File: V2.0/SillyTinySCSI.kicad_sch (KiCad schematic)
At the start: 26 parts, among them J1 DB25_Plug, U1 74LVT125, U2 74LVT245, U3 74LVT125, U4 74LVT245

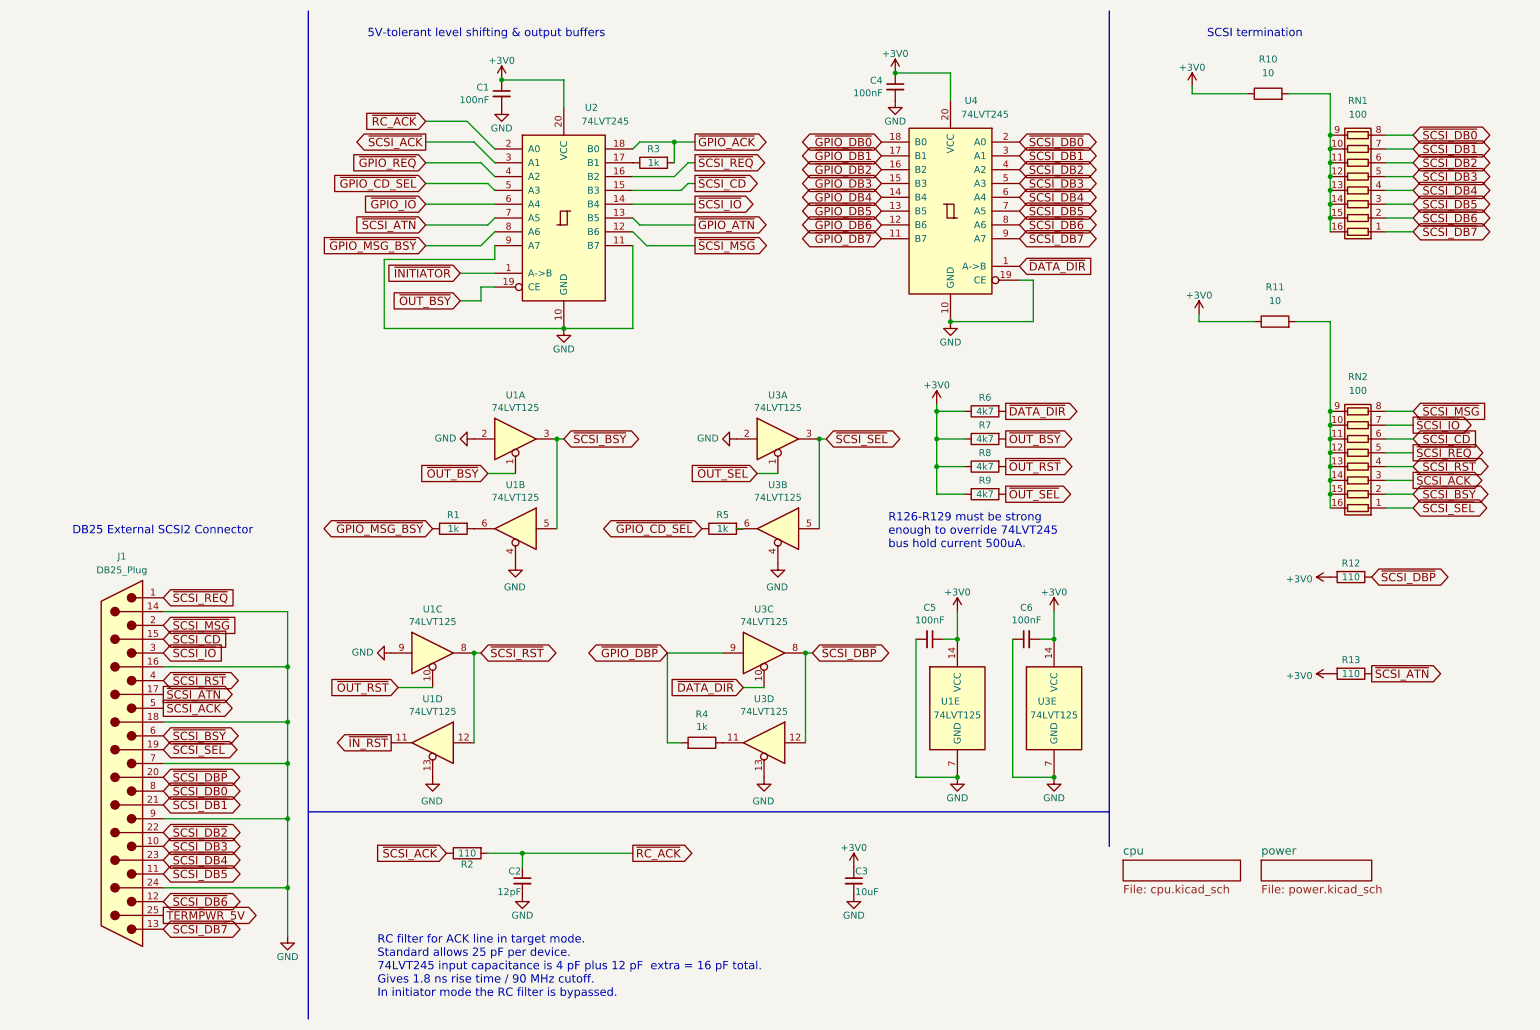
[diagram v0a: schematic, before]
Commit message: optimizations to buffers
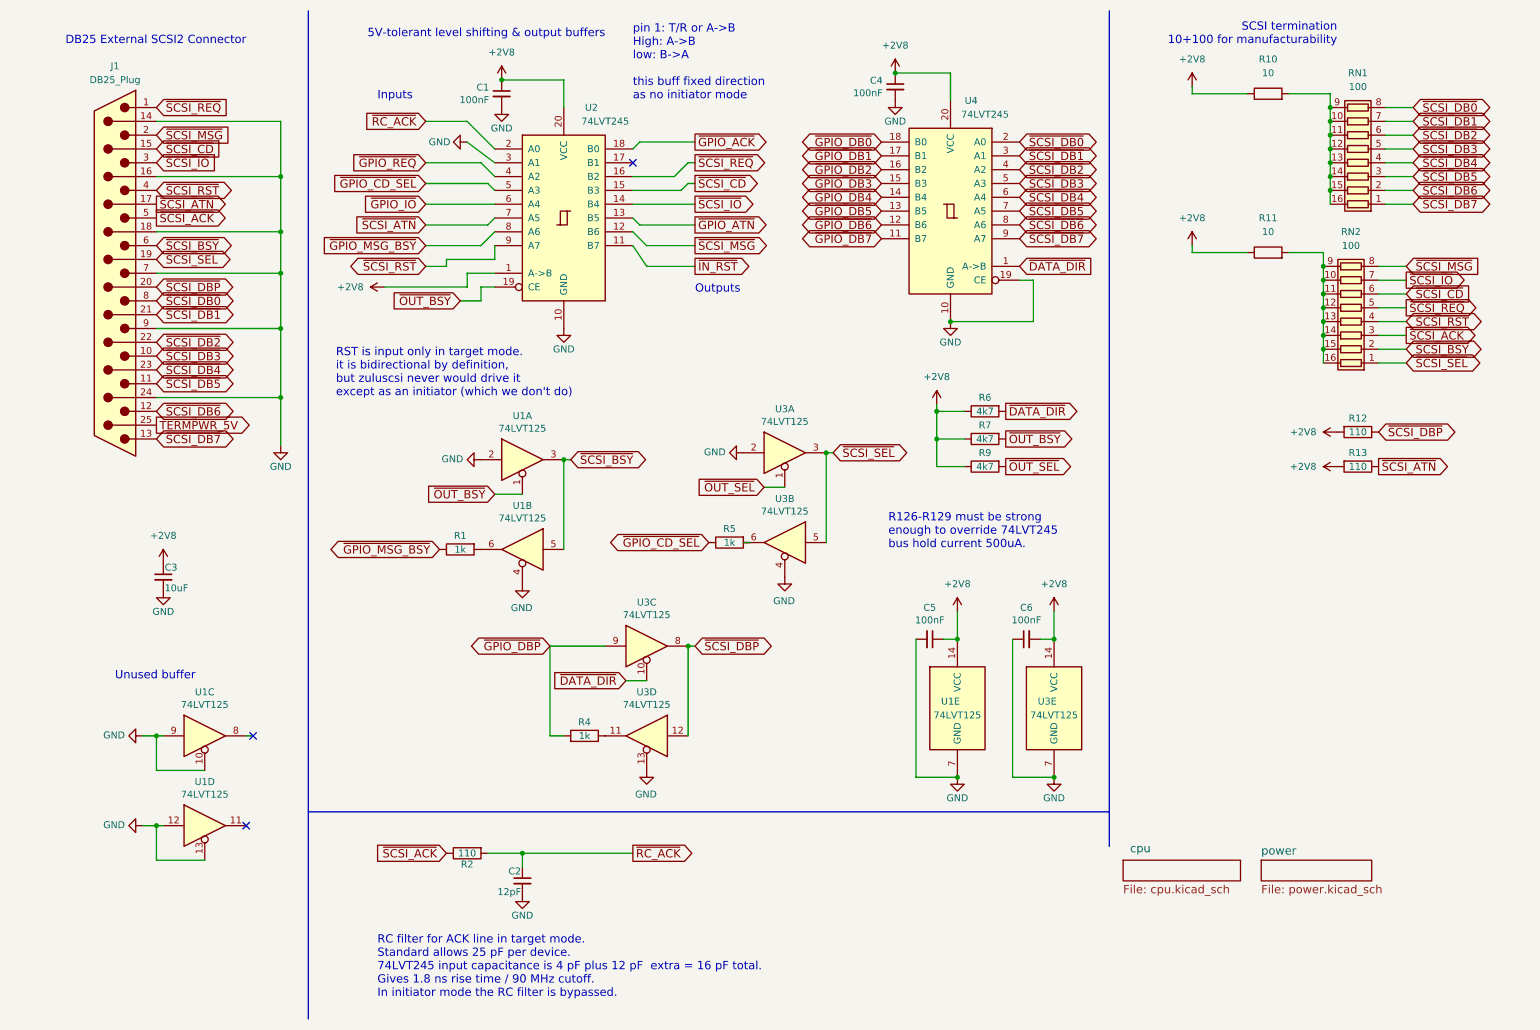
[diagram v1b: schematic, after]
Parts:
- removed R3: 1k, Resistor_SMD:R_0603_1608Metric, symbol zuluscsi-rescue:R
- removed R8: 4k7, Resistor_SMD:R_0603_1608Metric, symbol zuluscsi-rescue:R
- R10, R11: footprint Resistor_SMD:R_0603_1608Metric -> Resistor_SMD:R_1206_3216Metric; LCSC C22859 -> C727983; PartNumber 0603WAF100JT5E -> AC0805FR-7W10RL; digikey (none) -> 13-AC0805FR-7W10RLCT-ND
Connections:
- net ~{INITIATOR} is gone; now on net +2V8: U2.1 (A->B)
- net ~{OUT_RST} is gone; now on net GND: U1.10
- net GND: now also U1.12, U2.3 (A1); no longer U2.11 (B7), U2.9 (A7)
- net ~{IN_RST}: now also U2.11 (B7); no longer U1.11
- net ~{SCSI_ACK}: no longer U2.3 (A1)
- net ~{SCSI_RST}: now also U2.9 (A7); no longer U1.12, U1.8
- net +3V0 renamed +2V8
- no-connect marks 0 -> 3
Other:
- note added: "Inputs"
- note added: "Outputs"
- note added: "RST is input only in target mode. it is bidirectional by definition, but zuluscsi never would drive it except as an initiator (which we don't do)"
- note added: "SCSI termination 10+100 for manufacturability"
- note added: "Unused buffer"
- note added: "pin 1: T/R or A->B High: A->B low: B->A this buff fixed direction as no initiator mode"
- note removed: "SCSI termination"
- company: (C) Rabbit Hole Computing  -> ZZJ / M.D.
- title: ZuluSCSI (TM) Pico OSHW -> SillyTinySCSI
- moved on the sheet: C3, J1, R1, R11, R12, R13, R4, R5, R9, RN1, RN2, U1A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

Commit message: reverted some nuffer changes
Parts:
- R10, R11: LCSC C727983 -> C17903; PartNumber AC0805FR-7W10RL -> 1206W4F100JT5E; digikey 13-AC0805FR-7W10RLCT-ND -> RMCF1206JG10R0CT-ND
- RN1, RN2: digikey 13-YC248-JR-07100RLCT-ND -> RMCF0603FT51R0CT-ND - Cut Tape (CT)
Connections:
- net GND: now also U2.9 (A7); no longer U1.12
- net ~{IN_RST}: now also U1.11; no longer U2.11 (B7)
- net ~{SCSI_RST}: now also U1.12; no longer U2.9 (A7)
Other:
- note added: "Input"
- note added: "pin 1: T/R or A->B High: A->B low: B->A fixed direction as no initiator mode"
- note removed: "Inputs"
- note removed: "pin 1: T/R or A->B High: A->B low: B->A this buff fixed direction as no initiator mode"
- moved on the sheet: C3, R1, R4, R5, U1A, U1B, U1C, U3A, U3B, U3C, U3D

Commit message: last resistor pack
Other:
- moved on the sheet: C4

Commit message: before ar
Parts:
- removed R10, R11: 10, Resistor_SMD:R_1206_3216Metric, symbol Device:R
- removed RN1, RN2: 100, Resistor_SMD:R_Array_Convex_8x0602, symbol Device:R_Pack08
- added C14, C15: 10uF, Capacitor_SMD:C_0805_2012Metric, symbol zuluscsi-rescue:C_Small
- added R10, R11, R14, R21, R22, R23, R24, R25, R26, R27, R28, R29, R3, R30, R31, R8: 110, Resistor_SMD:R_0603_1608Metric, symbol zuluscsi-rescue:R
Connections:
- net +2V8: now also C14.1, C15.1, R10.2, R11.2, R14.2, R21.2, R22.2, R23.2, R24.2, R25.2, R26.2, R27.2, R28.2, R29.2, R3.2, R30.2, R31.2, R8.2
- net GND: now also C14.2, C15.2
- net ~{SCSI_ACK}: now also R21.1
- net ~{SCSI_BSY}: now also R22.1
- net ~{SCSI_CD}: now also R10.1
- net ~{SCSI_DB0}: now also R24.1
- net ~{SCSI_DB1}: now also R25.1
- net ~{SCSI_DB2}: now also R26.1
- net ~{SCSI_DB3}: now also R27.1
- net ~{SCSI_DB4}: now also R28.1
- net ~{SCSI_DB5}: now also R29.1
- net ~{SCSI_DB6}: now also R30.1
- net ~{SCSI_DB7}: now also R31.1
- net ~{SCSI_IO}: now also R8.1
- net ~{SCSI_MSG}: now also R3.1
- net ~{SCSI_REQ}: now also R11.1
- net ~{SCSI_RST}: now also R14.1
- net ~{SCSI_SEL}: now also R23.1
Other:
- note added: "SCSI termination"
- note removed: "SCSI termination 10+100 for manufacturability"
- moved on the sheet: C3

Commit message: rearrange
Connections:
- net ~{GPIO_DB4}: now also U4.11 (B7); no longer U4.14 (B4)
- net ~{GPIO_DB5}: now also U4.12 (B6); no longer U4.13 (B5)
- net ~{GPIO_DB6}: now also U4.13 (B5); no longer U4.12 (B6)
- net ~{GPIO_DB7}: now also U4.14 (B4); no longer U4.11 (B7)
- net ~{SCSI_DB4}: now also U4.9 (A7); no longer U4.6 (A4)
- net ~{SCSI_DB5}: now also U4.8 (A6); no longer U4.7 (A5)
- net ~{SCSI_DB6}: now also U4.7 (A5); no longer U4.8 (A6)
- net ~{SCSI_DB7}: now also U4.6 (A4); no longer U4.9 (A7)

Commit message: pwr routed
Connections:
- net ~{GPIO_DB4}: now also U4.14 (B4); no longer U4.11 (B7)
- net ~{GPIO_DB5}: now also U4.13 (B5); no longer U4.12 (B6)
- net ~{GPIO_DB6}: now also U4.12 (B6); no longer U4.13 (B5)
- net ~{GPIO_DB7}: now also U4.11 (B7); no longer U4.14 (B4)
- net ~{SCSI_DB4}: now also U4.6 (A4); no longer U4.9 (A7)
- net ~{SCSI_DB5}: now also U4.7 (A5); no longer U4.8 (A6)
- net ~{SCSI_DB6}: now also U4.8 (A6); no longer U4.7 (A5)
- net ~{SCSI_DB7}: now also U4.9 (A7); no longer U4.6 (A4)

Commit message: sync up
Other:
- moved on the sheet: C3
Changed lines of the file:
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@@
     )
   )
-  (symbol (lib_id "zuluscsi-rescue:C_Small") (at 233.68 114.3 0) (unit 1)
-    (in_bom yes) (on_board yes) (dnp no)
-    (property "Reference" "C3" (at 233.934 112.522 0)
+  (symbol (lib_id "zuluscsi-rescue:C_Small") (at 38.1 127 0) (unit 1)
+    (in_bom yes) (on_board yes) (dnp no)
+    (property "Reference" "C3" (at 38.354 125.222 0)
       (effects (font (size 1.27 1.27)) (justify left))
     )
-    (property "Value" "10uF" (at 233.934 116.332 0)
+    (property "Value" "10uF" (at 38.354 129.032 0)
       (effects (font (size 1.27 1.27)) (justify left))
     )
-    (property "Footprint" "Capacitor_SMD:C_0805_2012Metric" (at 233.68 114.3 0)
+    (property "Footprint" "Capacitor_SMD:C_0805_2012Metric" (at 38.1 127 0)
       (effects (font (size 1.524 1.524)) hide)
     )
-    (property "Datasheet" "" (at 233.68 114.3 0)
-      (effects (font (size 1.524 1.524)))
-    )
-    (property "LCSC" "C15850" (at 233.68 114.3 0)
-      (effects (font (size 1.27 1.27)) hide)
-    )
-    (property "Manufacturer" "Samsung" (at 233.68 114.3 0)
-      (effects (font (size 1.27 1.27)) hide)
-    )
-    (property "PartNumber" "CL21A106KPFNNNG" (at 233.68 114.3 0)
-      (effects (font (size 1.27 1.27)) hide)
-    )
-    (property "digikey" "1276-6456-1-ND " (at 233.68 114.3 0)
-      (effects (font (size 1.27 1.27)) hide)
-    )
-    (property "JLCPCBCORRECT" "" (at 233.68 114.3 0)
-      (effects (font (size 1.27 1.27)) hide)
-    )
-    (property "JLCPCB_IGNORE" "" (at 233.68 114.3 0)
+    (property "Datasheet" "" (at 38.1 127 0)
+      (effects (font (size 1.524 1.524)))
+    )
+    (property "LCSC" "C15850" (at 38.1 127 0)
+      (effects (font (size 1.27 1.27)) hide)
+    )
+    (property "Manufacturer" "Samsung" (at 38.1 127 0)
+      (effects (font (size 1.27 1.27)) hide)
+    )
+    (property "PartNumber" "CL21A106KPFNNNG" (at 38.1 127 0)
+      (effects (font (size 1.27 1.27)) hide)
+    )
+    (property "digikey" "1276-6456-1-ND " (at 38.1 127 0)
+      (effects (font (size 1.27 1.27)) hide)
+    )
+    (property "JLCPCBCORRECT" "" (at 38.1 127 0)
+      (effects (font (size 1.27 1.27)) hide)
+    )
+    (property "JLCPCB_IGNORE" "" (at 38.1 127 0)
       (effects (font (size 1.27 1.27)) hide)
     )
@@
     )
   )
-  (symbol (lib_id "zuluscsi-rescue:GND") (at 233.68 116.84 0) (unit 1)
-    (in_bom yes) (on_board yes) (dnp no)
-    (property "Reference" "#PWR014" (at 233.68 123.19 0)
-      (effects (font (size 1.27 1.27)) hide)
-    )
-    (property "Value" "GND" (at 233.68 120.65 0)
-      (effects (font (size 1.27 1.27)))
-    )
-    (property "Footprint" "" (at 233.68 116.84 0)
-      (effects (font (size 1.524 1.524)))
-    )
-    (property "Datasheet" "" (at 233.68 116.84 0)
+  (symbol (lib_id "zuluscsi-rescue:GND") (at 38.1 129.54 0) (unit 1)
+    (in_bom yes) (on_board yes) (dnp no)
+    (property "Reference" "#PWR014" (at 38.1 135.89 0)
+      (effects (font (size 1.27 1.27)) hide)
+    )
+    (property "Value" "GND" (at 38.1 133.35 0)
+      (effects (font (size 1.27 1.27)))
+    )
+    (property "Footprint" "" (at 38.1 129.54 0)
+      (effects (font (size 1.524 1.524)))
+    )
+    (property "Datasheet" "" (at 38.1 129.54 0)
       (effects (font (size 1.524 1.524)))
     )
@@
     )
   )
-  (symbol (lib_id "power:+2V8") (at 233.68 111.76 0) (unit 1)
+  (symbol (lib_id "power:+2V8") (at 38.1 124.46 0) (unit 1)
     (in_bom yes) (on_board yes) (dnp no) (fields_autoplaced)
-    (property "Reference" "#PWR044" (at 233.68 115.57 0)
-      (effects (font (size 1.27 1.27)) hide)
-    )
-    (property "Value" "+2V8" (at 233.68 106.68 0)
-      (effects (font (size 1.27 1.27)))
-    )
-    (property "Footprint" "" (at 233.68 111.76 0)
-      (effects (font (size 1.27 1.27)) hide)
-    )
-    (property "Datasheet" "" (at 233.68 111.76 0)
-      (effects (font (size 1.27 1.27)) hide)
-    )
+    (property "Reference" "#PWR044" (at 38.1 128.27 0)
+      (effects (font (size 1.27 1.27)) hide)
+    )
+    (property "Value" "+2V8" (at 38.1 119.38 0)
+      (effects (font (size 1.27 1.27)))
+    )
+    (property "Footprint" "" (at 38.1 124.46 0)
+      (effects (font (size 1.27 1.27)) hide)
+    )
+    (property "Datasheet" "" (at 38.1 124.46 0)
+      (effects (font (size 1.27 1.27)) hide)
+    )

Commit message: bring current
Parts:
- removed unit 3 of U1
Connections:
- no-connect marks 3 -> 2
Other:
- note removed: "Unused buffer"
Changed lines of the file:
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@@
   (junction (at 247.65 40.64) (diameter 0) (color 0 0 0 0)
   )
-  (junction (at 36.83 168.91) (diameter 0) (color 0 0 0 0)
-  )
   (junction (at 184.15 153.67) (diameter 0) (color 0 0 0 0)
   )
@@
   (junction (at 247.65 38.1) (diameter 0) (color 0 0 0 0)
   )
-  (no_connect (at 54.61 168.91))
   (no_connect (at 124.46 55.88))
   (no_connect (at 124.46 40.64))
@@
     (stroke (width 0) (type default))
   )
-  (wire (pts (xy 54.61 168.91) (xy 53.34 168.91))
-    (stroke (width 0) (type default))
-  )
   (wire (pts (xy 261.62 43.18) (xy 266.7 43.18))
     (stroke (width 0) (type default))
@@
     (stroke (width 0) (type default))
   )
-  (wire (pts (xy 34.29 168.91) (xy 36.83 168.91))
-    (stroke (width 0) (type default))
-  )
   (wire (pts (xy 125.73 36.83) (xy 135.89 36.83))
     (stroke (width 0) (type default))
@@
     (stroke (width 0) (type default))
   )
-  (wire (pts (xy 36.83 175.26) (xy 36.83 168.91))
-    (stroke (width 0) (type default))
-  )
   (wire (pts (xy 176.53 128.27) (xy 176.53 153.67))
     (stroke (width 0) (type default))
@@
     (stroke (width 0) (type default))
   )
-  (wire (pts (xy 36.83 168.91) (xy 38.1 168.91))
-    (stroke (width 0) (type default))
-  )
   (wire (pts (xy 237.49 27.94) (xy 240.03 27.94))
     (stroke (width 0) (type default))
@@
     (stroke (width 0) (type default))
   )
-  (wire (pts (xy 45.72 175.26) (xy 36.83 175.26))
-    (stroke (width 0) (type default))
-  )
   (wire (pts (xy 261.62 69.85) (xy 266.7 69.85))
     (stroke (width 0) (type default))
@@
     (effects (font (size 1.524 1.524)) (justify right bottom))
   )
-  (text "Unused buffer" (at 29.21 158.75 0)
-    (effects (font (size 1.524 1.524)) (justify left bottom))
-  )
   (text "RST is input only in target mode.\nit is bidirectional by definition, \nbut zuluscsi never would drive it\nexcept as an initiator (which we don't do)"
     (at 71.12 154.94 0)
@@
     )
   )
-  (symbol (lib_id "74xx:74LVC125") (at 45.72 168.91 0) (unit 3)
-    (in_bom yes) (on_board yes) (dnp no)
-    (property "Reference" "U1" (at 45.72 160.8582 0)
-      (effects (font (size 1.27 1.27)))
-    )
-    (property "Value" "74LVT125" (at 45.72 163.1696 0)
-      (effects (font (size 1.27 1.27)))
-    )
-    (property "Footprint" "ZuluSCSI:SSOP_TSSOP-14_4.4x5mm_Pitch0.65mm_PCBWay-MaskClearance0.22mm" (at 45.72 168.91 0)
-      (effects (font (size 1.27 1.27)) hide)
-    )
-    (property "Datasheet" "http://www.ti.com/lit/gpn/sn74LVC125" (at 45.72 168.91 0)
-      (effects (font (size 1.27 1.27)) hide)
-    )
-    (property "LCSC" "C7042" (at 45.72 168.91 0)
-      (effects (font (size 1.27 1.27)) hide)
-    )
-    (property "Manufacturer" "Onsemi" (at 45.72 168.91 0)
-      (effects (font (size 1.27 1.27)) hide)
-    )
-    (property "PartNumber" "74LVTH125MTC" (at 45.72 168.91 0)
-      (effects (font (size 1.27 1.27)) hide)
-    )
-    (property "digikey" "74LVTH125MTC-ND" (at 45.72 168.91 0)
-      (effects (font (size 1.27 1.27)) hide)
-    )
-    (property "JLCPCBCORRECT" "0;0;-90" (at 45.72 168.91 0)
-      (effects (font (size 1.27 1.27)) hide)
-    )
-    (property "JLCPCB_IGNORE" "" (at 45.72 168.91 0)
-      (effects (font (size 1.27 1.27)) hide)
-    )
-    (pin "1")
-    (pin "2")
-    (pin "3")
-    (pin "4")
-    (pin "5")
-    (pin "6")
-    (pin "10")
-    (pin "8")
-    (pin "9")
-    (pin "11")
-    (pin "12")
-    (pin "13")
-    (pin "14")
-    (pin "7")
-    (instances
-      (project "SillyTinySCSI"
-        (path "/0a1a4d88-972a-46ce-b25e-6cb796bd41f7"
-          (reference "U1") (unit 3)
-        )
-      )
-    )
-  )
   (symbol (lib_id "zuluscsi-rescue:R") (at 257.81 67.31 270) (unit 1)
     (in_bom yes) (on_board yes) (dnp no)
@@
         )
       )
-    )
-  )
-  (symbol (lib_id "zuluscsi-rescue:GND") (at 34.29 168.91 270) (mirror x) (unit 1)
-    (in_bom yes) (on_board yes) (dnp no)
-    (property "Reference" "#PWR02" (at 27.94 168.91 0)
-      (effects (font (size 1.27 1.27)) hide)
-    )
-    (property "Value" "GND" (at 31.0388 168.783 90)
-      (effects (font (size 1.27 1.27)) (justify right))
-    )
-    (property "Footprint" "" (at 34.29 168.91 0)
-      (effects (font (size 1.27 1.27)) hide)
-    )
-    (property "Datasheet" "" (at 34.29 168.91 0)
-      (effects (font (size 1.27 1.27)) hide)
-    )
-    (pin "1")
-    (instances
-      (project "SillyTinySCSI"
-        (path "/0a1a4d88-972a-46ce-b25e-6cb796bd41f7"
-          (reference "#PWR02") (unit 1)
-        )
-      )
